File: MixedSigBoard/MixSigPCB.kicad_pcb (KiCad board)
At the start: 4 copper layers, 58.3 x 75.8 mm, 114 parts, among them J200 2x5 1.27mm, J201 USB_C_Receptacle_USB2.0, J300 031-5640-1010, J400 031-5640-1010, U100 TLV62569DBV, U101 HT7533-1, U102 MCP6001T-E/OT, U200 STM32F103CBT6, U201 USBLC6-2SC6, U300 REF3033AIDBZT, U301 ADC141S626CIMM_NOPB, U302 MCP6001T-E/OT, U303 MCP6001T-E/OT, U400 DAC7563SDGSR, U401 MCP6001T-E/OT, Y200 16MHz

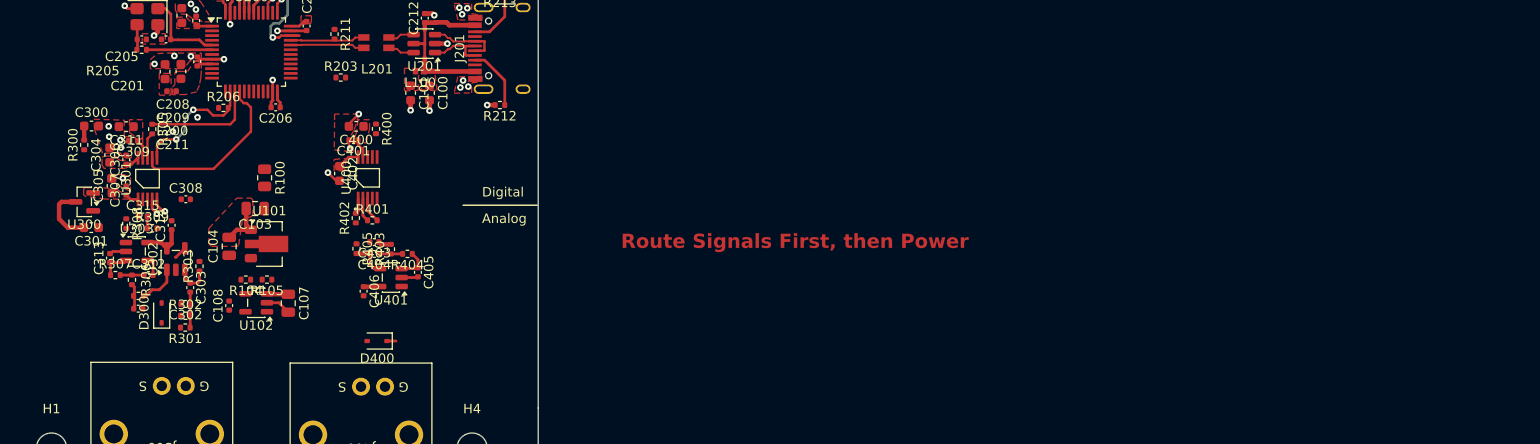
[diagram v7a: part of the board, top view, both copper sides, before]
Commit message: add routing for 1 of 2 analog portions
- 50 ohm trace routing for analog portion
- adc portion routing finished (except POWER routing)
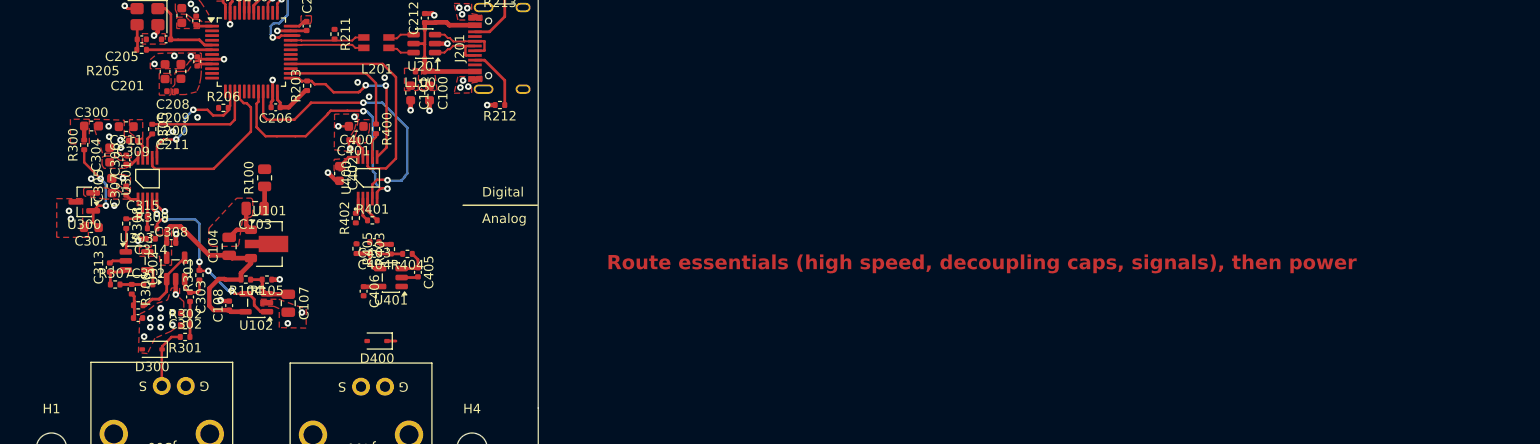
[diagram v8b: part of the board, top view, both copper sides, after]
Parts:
- moved C308 4.88 mm to (47.2, 62.5)
- moved D300 3.98 mm to (45.1, 73.8), turned to 180 degrees
- moved R203 3.66 mm to (61.5, 45.9), turned to 90 degrees
- moved C314 2.63 mm to (45.0, 62.1), turned to 180 degrees
- moved C302 0.99 mm to (48.7, 70.0)
- moved C303 0.99 mm to (49.2, 68.3)
- moved C310 0.99 mm to (43.7, 70.5)
- moved C312 0.99 mm to (44.7, 66.9)
- moved C313 0.99 mm to (40.7, 65.1)
- moved R301 0.99 mm to (48.6, 72.5)
- moved R302 0.99 mm to (48.7, 71.2)
- moved R304 0.99 mm to (43.7, 69.1)
- moved R306 0.99 mm to (43.0, 67.4)
- moved R307 0.99 mm to (41.2, 66.9)
- moved U302 0.99 mm to (47.6, 65.2)
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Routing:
- net DAC_NLDAC: track 0.00 -> 30.6 mm, vias 0 -> 2
- net DAC_NCLR: track 0.00 -> 28.6 mm, vias 0 -> 2
- net SPI2_MOSI: track 0.00 -> 24.8 mm
- net +3.3VA: track 7.76 -> 27.6 mm
- net VCOM: track 0.00 -> 19.6 mm, vias 0 -> 4
- net SPI2_NSS: track 0.00 -> 19.5 mm, vias 0 -> 2
- net SPI2_SCK: track 0.00 -> 13.8 mm
- net /ADC/ADC_VREF_VIN: track 0.00 -> 10.5 mm, vias 0 -> 2
- net /ADC/IN: track 0.00 -> 6.53 mm
- net GND: track 67.3 -> 63.0 mm, vias 46 -> 69
- net +3V3: track 15.2 -> 18.8 mm
- net /ADC/ADC_IN+: track 0.00 -> 3.38 mm
- net /Power/VREF: track 2.27 -> 5.20 mm
- net /ADC/IN_AA_BUF_OUT: track 2.15 -> 4.82 mm
- net /DAC/DAC_SCLK: track 0.00 -> 2.63 mm
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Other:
- board text added: "Route essentials (high speed, decoupling caps, signals), then power"
- board text removed: "Route Signals First, then Power"
